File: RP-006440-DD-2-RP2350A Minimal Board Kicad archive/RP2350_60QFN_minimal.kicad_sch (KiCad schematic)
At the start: 43 parts, among them J1 USB_B_Micro, J2 Conn_02x18_Odd_Even, J3 Conn_02x18_Odd_Even, J4 SM03B-SRSS-TB, SW1 SW_Push, SW2 SW_Push, U1 RP2350_60QFN, U2 NCP1117-3.3_SOT223, U3 W25Q128JVS, Y1 ABM8-272-T3

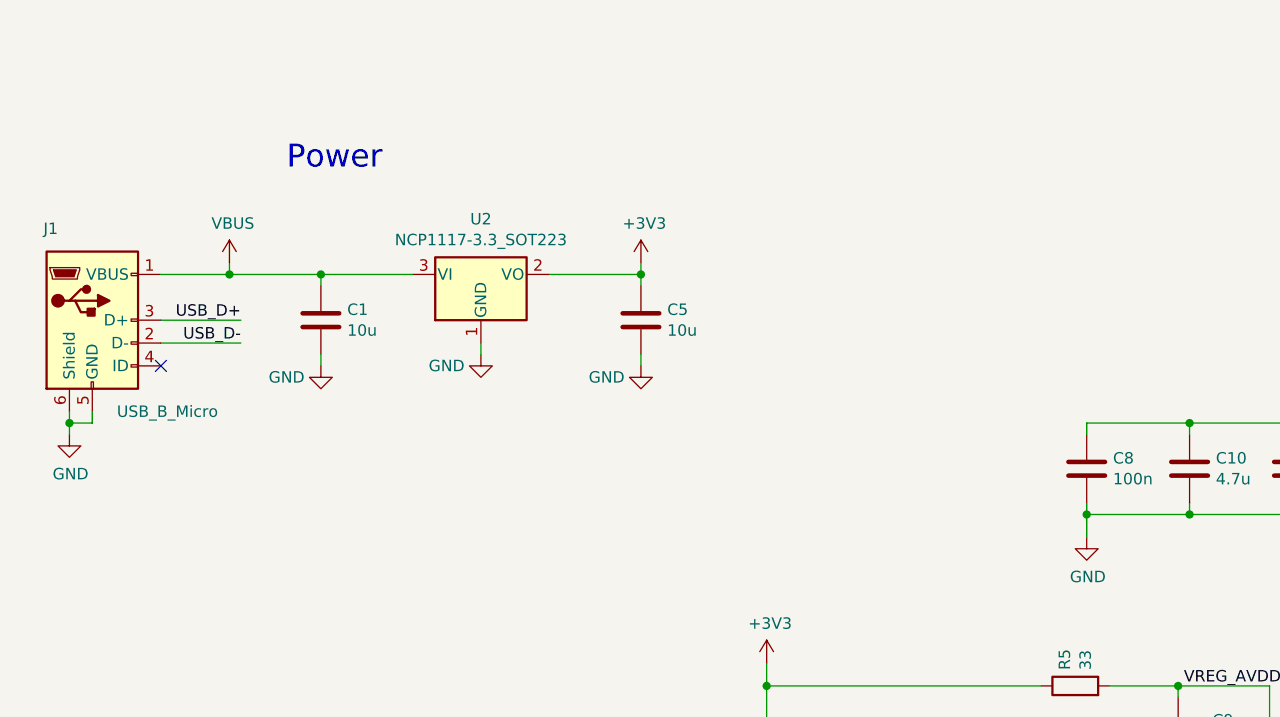
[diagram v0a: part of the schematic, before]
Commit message: USB-C schematic
replaced micro usb schematic with usb 2.0 type c plus 5.1k resistors on CC1/2
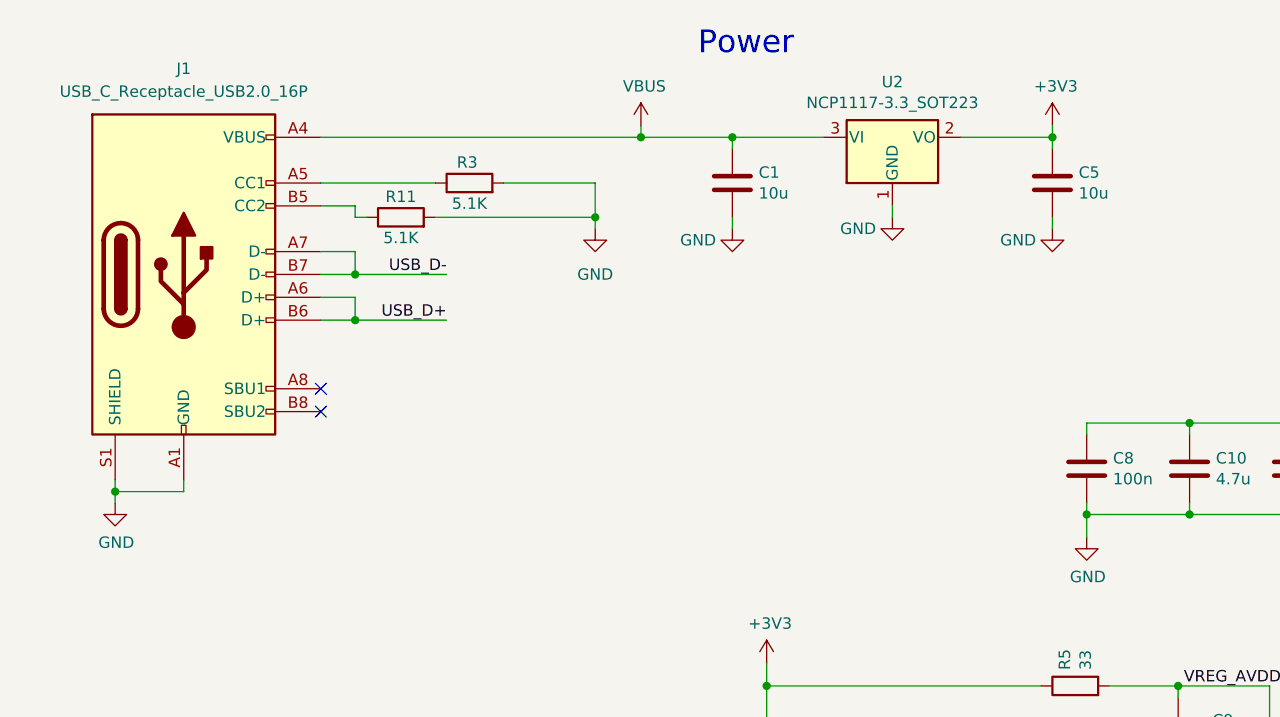
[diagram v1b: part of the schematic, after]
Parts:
- removed J1: USB_B_Micro, Connector_USB:USB_Micro-B_Amphenol_10103594-0001LF_Horizontal, symbol Connector:USB_B_Micro
- added J1: USB_C_Receptacle_USB2.0_16P, Connector_USB:USB_C_Receptacle_HRO_TYPE-C-31-M-12, symbol Connector:USB_C_Receptacle_USB2.0_16P
- added R11, R3: 5.1K, symbol Device:R
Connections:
- net GND: now also J1.A1 (GND), J1.A12 (GND), J1.B1 (GND), J1.B12 (GND), J1.S1 (SHIELD), R11.2, R3.2
- net USB_D+: now also J1.A6 (D+), J1.B6 (D+)
- net USB_D-: now also J1.A7 (D-), J1.B7 (D-)
- net VBUS: now also J1.A4 (VBUS), J1.A9 (VBUS), J1.B4 (VBUS), J1.B9 (VBUS)
- new net: J1.B5 (CC2), R11.1
- new net: J1.A5 (CC1), R3.1
- no-connect marks 1 -> 2
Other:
- moved on the sheet: C1, C5, U2
